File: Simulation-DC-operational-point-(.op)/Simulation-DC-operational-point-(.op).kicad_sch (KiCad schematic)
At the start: 3 parts

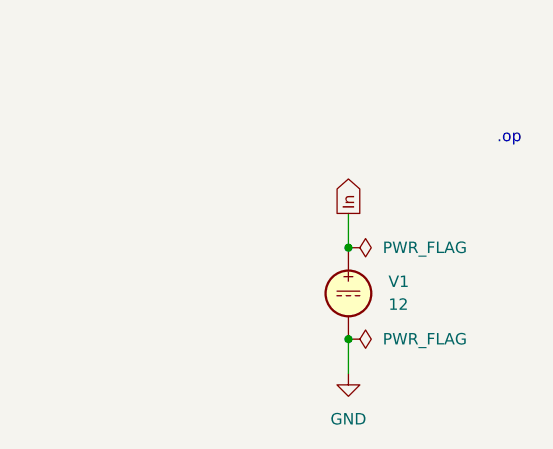
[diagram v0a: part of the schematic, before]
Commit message: Updated all schematics and prepared for KiCad 8.0
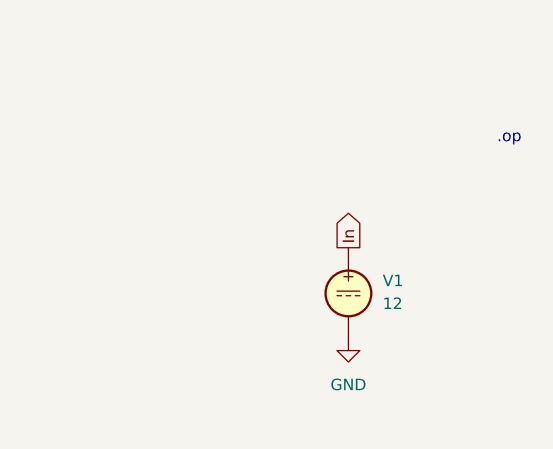
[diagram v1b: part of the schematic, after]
